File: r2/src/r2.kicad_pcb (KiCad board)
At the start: 4 copper layers, 110.2 x 145.8 mm, 234 parts, among them J1 532610271, J10 PJ-320D, J2 USB-C-12, J3 UJ2-AH-1-SMT, J4 TF-15x15, J5 AFC07-S24ECA-00, J6 DNP, J7 2x03-socket-2.54-through-board, J8 DNP, J9 532610271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

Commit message: Fabricate. End of history
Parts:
- moved FID1 22.8 mm to (-48.0, -129.4)
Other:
- board text added: "banellick"
- board text added: "jeffmakes"
- board text added: "malte"
- board text added: "norbert"
- board text added: "sourcing : nick completion : na origin : critical tooling : critical knowledge : critical understanding : unnecessary understanding : critical art : critical platform : mixed substrate : mixed credit : powers of two design ltd. custom : ernw insight gmbh. vendor : monad gottfried ltd., london assurance : critical opsec : redacted concept : critical synthesis : monad order : critical legal : gottf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"

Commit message: Remove stackup definition which was preventing file from  opening in my version of  kicad, for some unexplained reason
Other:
- board text added: "sourcing : nick origin : critical tooling : critical understanding : unnecessary understanding : critical art : critical platform : mixed substrate : mixed credit : powers of two design ltd. custom : ernw insight gmbh. vendor : monad gottfried ltd., london assurance : critical opsec : redacted concept : critical synthesis : monad legal : gottfried risk : powers of two design ltd. london support :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"
- board text removed: "sourcing : nick completion : na origin : critical tooling : critical knowledge : critical understanding : unnecessary understanding : critical art : critical platform : mixed substrate : mixed credit : powers of two design ltd. custom : ernw insight gmbh. vendor : monad gottfried ltd., london assurance : critical opsec : redacted concept : critical synthesis : monad order : critical legal : gottf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"

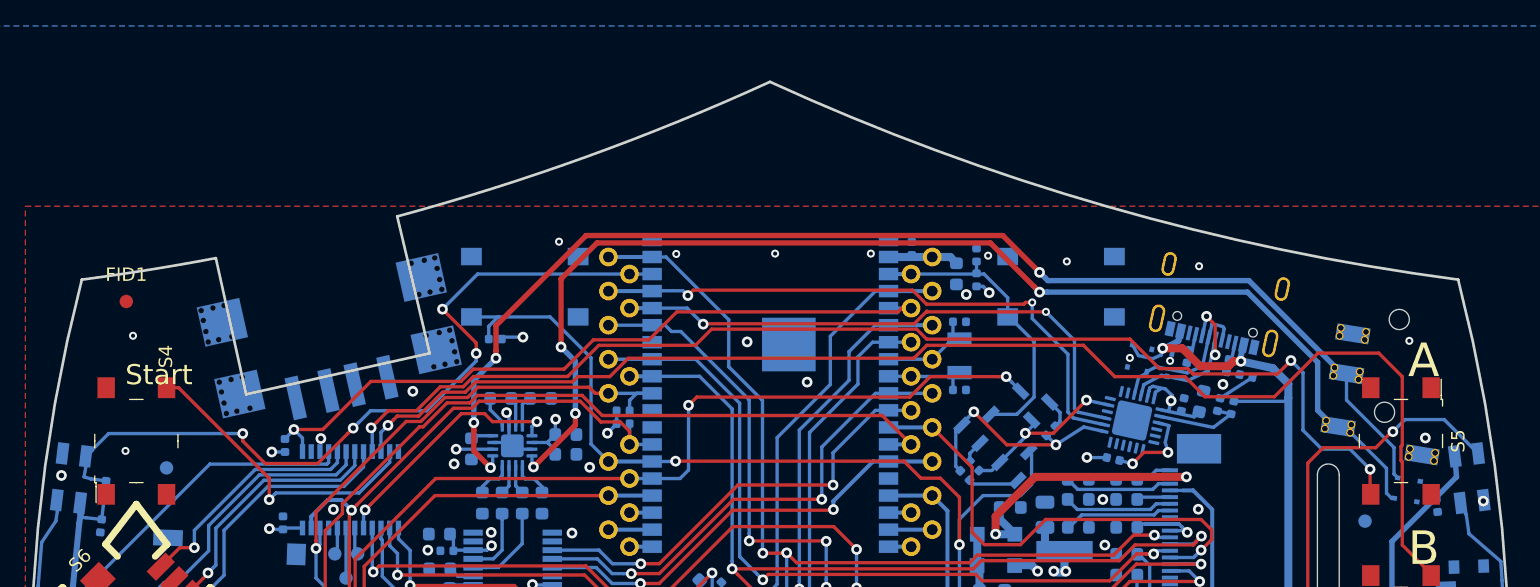
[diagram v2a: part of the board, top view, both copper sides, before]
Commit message: Updated USB-A footprint, board edge corrected to match
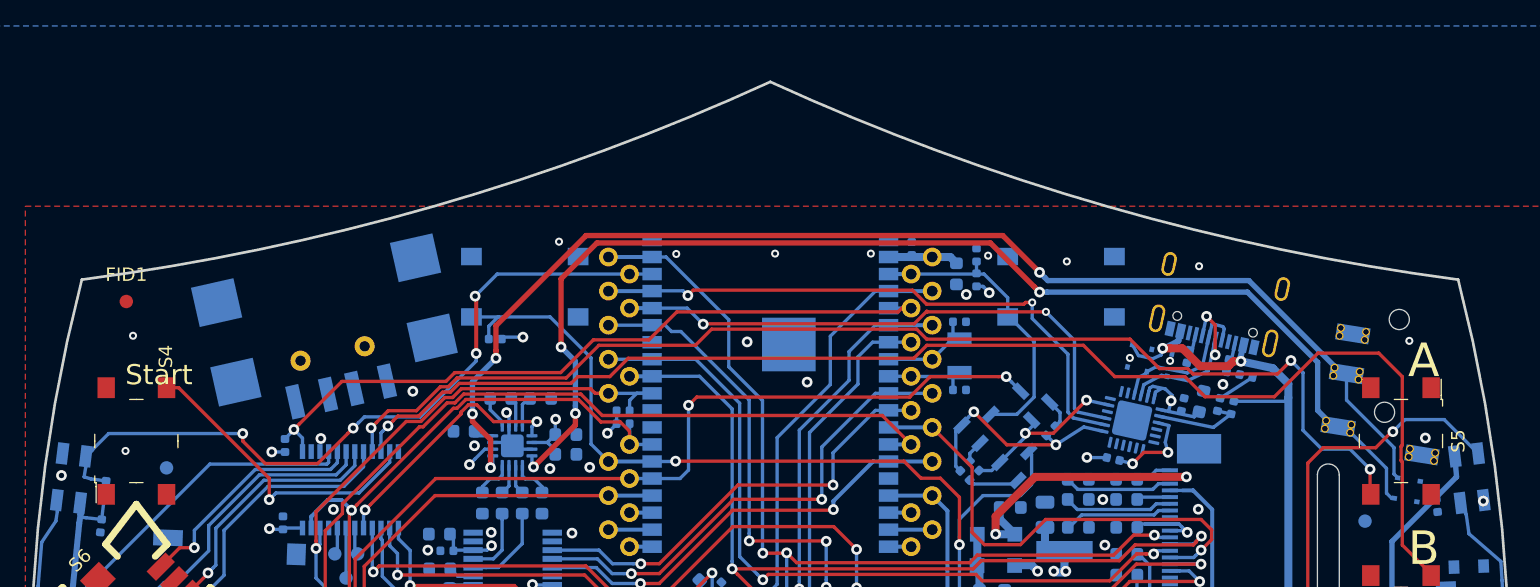
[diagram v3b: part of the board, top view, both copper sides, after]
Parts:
- J3: footprint jeffmakes-footprints:USB-A-short-body-in-cutout-type -> jeffmakes-footprints:USB-A-short-body
- moved J3 8.57 mm to (-32.6, -125.5)
- moved C87 1.42 mm to (-22.8, -119.7), turned to 0 degrees
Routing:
- net /LED_DIN: track 60.0 -> 57.4 mm
- net /AMP_EN: track 18.6 -> 19.2 mm
- net +3V3: track 1362.1 -> 1361.6 mm
- net GND: vias 168 -> 169
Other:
- outline, holes or cut-outs redrawn

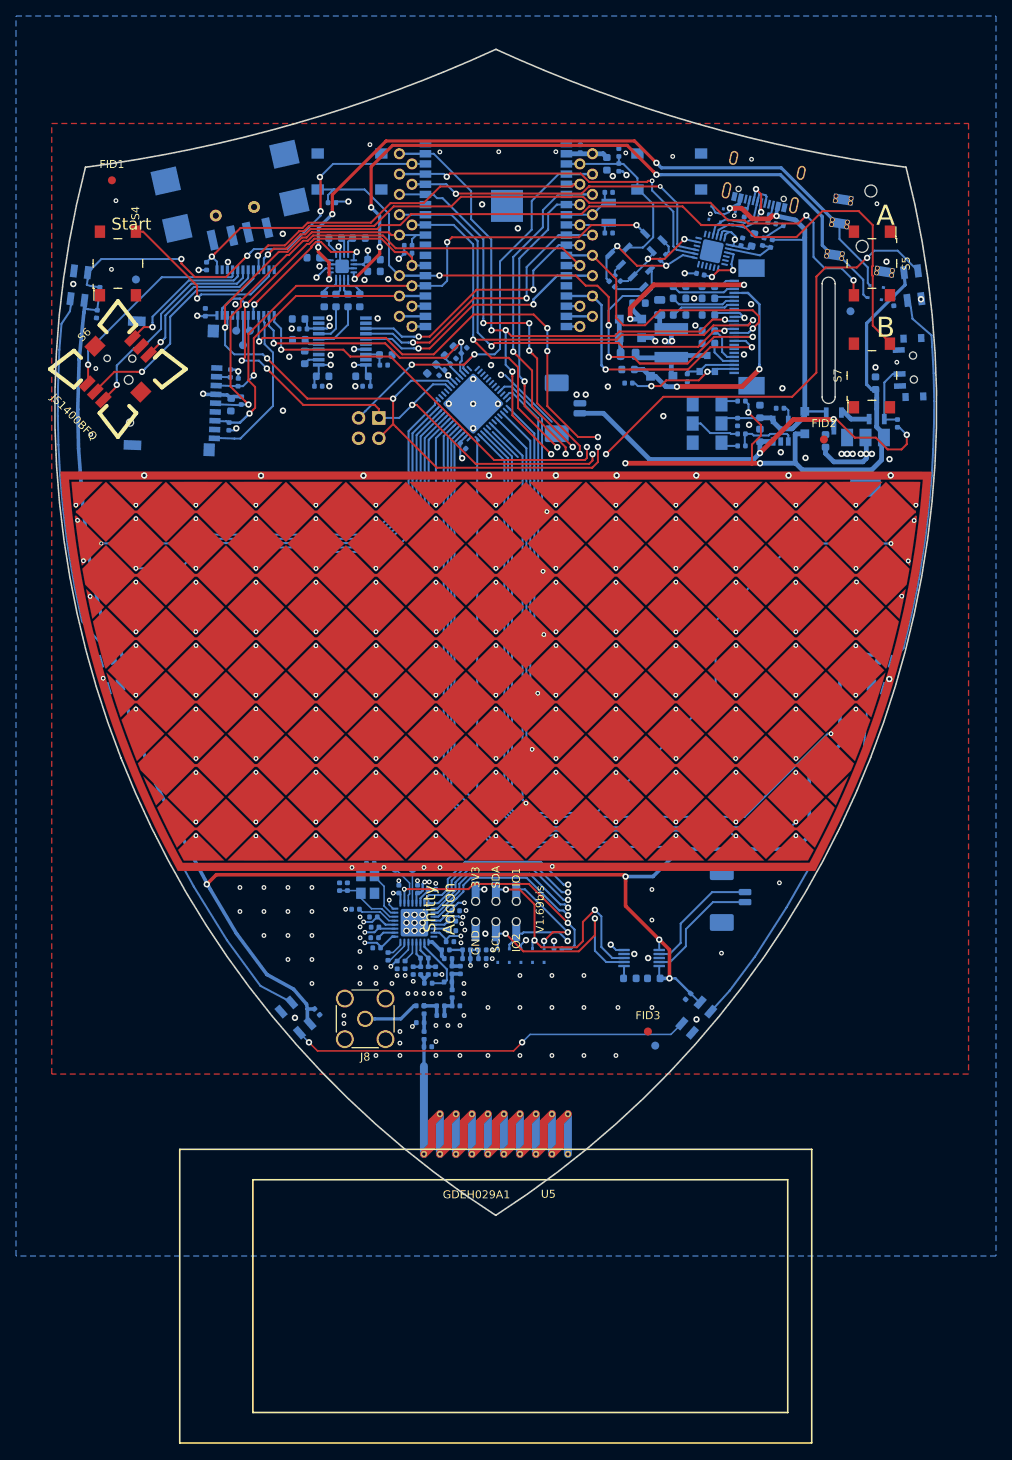
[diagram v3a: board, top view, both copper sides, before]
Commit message: DRC pass, silk for SAO
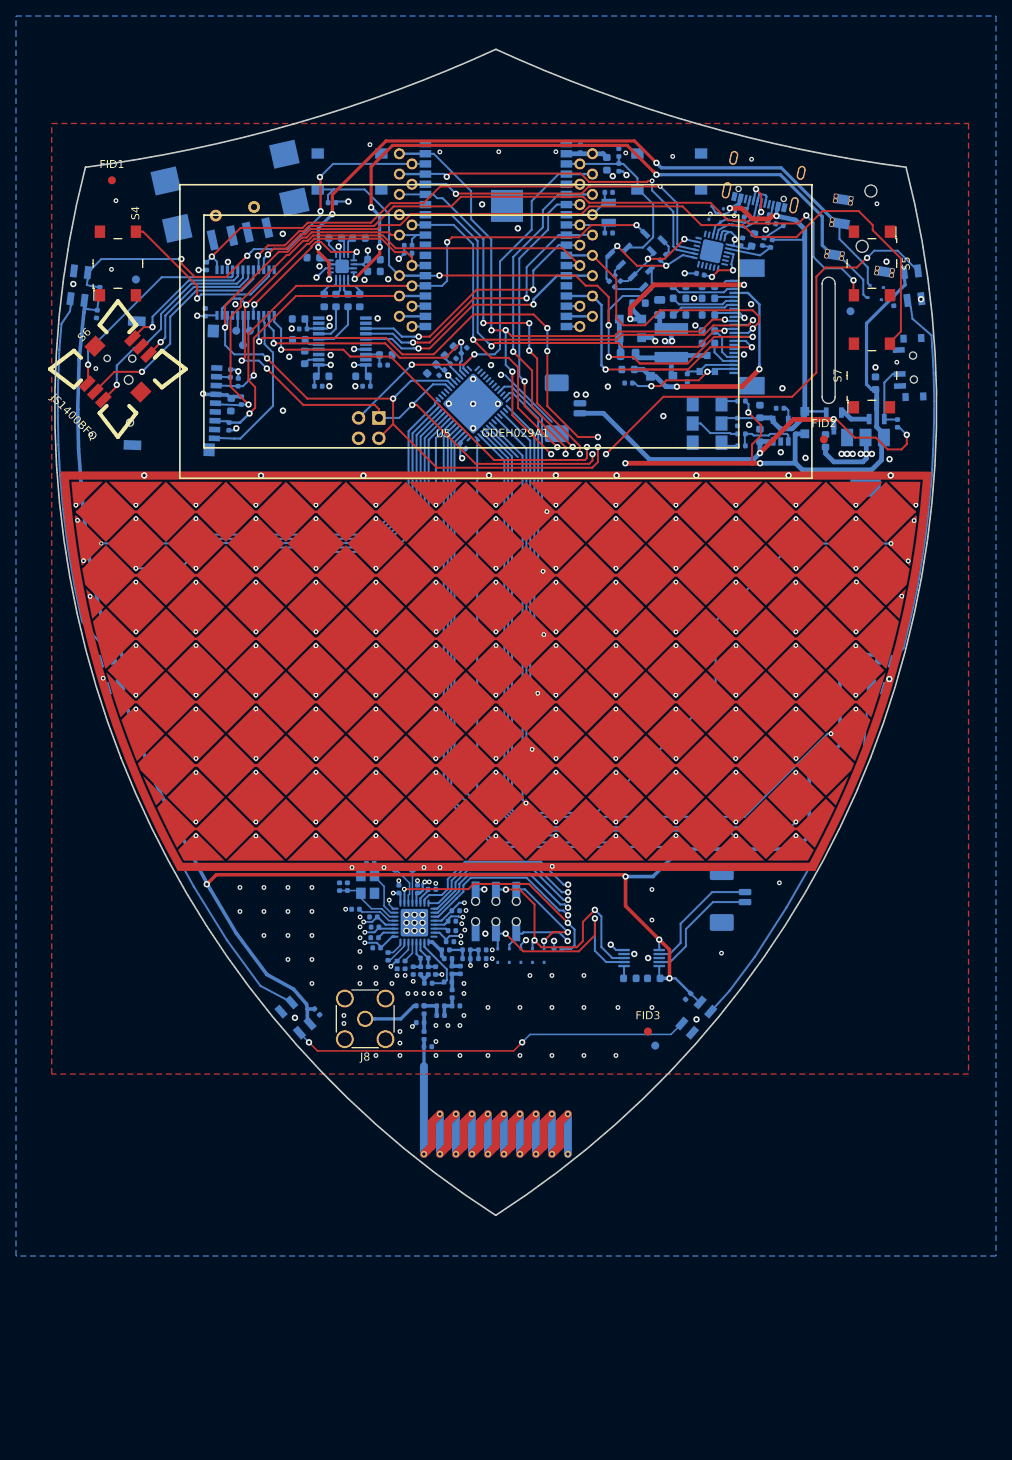
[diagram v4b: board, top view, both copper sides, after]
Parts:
- moved U5 120.6 mm to (0.00, -110.5), turned to 180 degrees
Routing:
- net /io_expander/BTN_B: track 99.7 -> 100.9 mm
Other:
- board text removed: "A"
- board text removed: "B"
- board text removed: "Start"

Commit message: Add credits
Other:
- board text added: "credits: badge.team norbert dr kl jim rgilton nick celina"
- board text removed: "banellick"
- board text removed: "jeffmakes"
- board text removed: "malte"
- board text removed: "norbert"
- board text removed: "sourcing : nick origin : critical tooling : critical understanding : unnecessary understanding : critical art : critical platform : mixed substrate : mixed credit : powers of two design ltd. custom : ernw insight gmbh. vendor : monad gottfried ltd., london assurance : critical opsec : redacted concept : critical synthesis : monad legal : gottfried risk : powers of two design ltd. london support :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"
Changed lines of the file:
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@@
   (general
     (thickness 1.6)
-    (drawings 87)
+    (drawings 60)
     (tracks 2399)
     (modules 234)
@@
     (32 "B.Adhes" user hide)
     (33 "F.Adhes" user hide)
-    (34 "B.Paste" user)
+    (34 "B.Paste" user hide)
     (35 "F.Paste" user hide)
     (36 "B.SilkS" user)
@@
     (45 "Margin" user hide)
     (46 "B.CrtYd" user hide)
-    (47 "F.CrtYd" user hide)
-    (48 "B.Fab" user hide)
-    (49 "F.Fab" user)
+    (47 "F.CrtYd" user)
+    (48 "B.Fab" user)
+    (49 "F.Fab" user hide)
   )
   (setup
@@
   )
   (gr_curve (pts (xy -51.312409 -131.029767) (xy -33.555051 -133.367724) (xy -16.268868 -138.335922) (xy 0 -145.7706)) (layer "Edge.Cuts") (width 0.2))
-  (gr_text "banellick" (at 0.8 -29) (layer "In1.Cu")
-    (effects (font (size 1 1) (thickness 0.1)) (justify mirror))
-  )
-  (gr_text "banellick" (at -25.8 -39.6) (layer "In1.Cu")
-    (effects (font (size 1 1) (thickness 0.1)) (justify mirror))
-  )
-  (gr_text "banellick" (at 19.8 -39) (layer "In1.Cu")
-    (effects (font (size 1 1) (thickness 0.1)) (justify mirror))
-  )
-  (gr_text "malte" (at 9.4 -31.6) (layer "In1.Cu")
-    (effects (font (size 1 1) (thickness 0.1)) (justify mirror))
-  )
-  (gr_text "malte" (at -20.2 -30.4) (layer "In1.Cu")
-    (effects (font (size 1 1) (thickness 0.1)) (justify mirror))
-  )
-  (gr_text "malte" (at -44.2 -125.4) (layer "In1.Cu")
-    (effects (font (size 1 1) (thickness 0.1)) (justify mirror))
-  )
-  (gr_text "malte" (at -38.8 -105.6) (layer "In1.Cu")
-    (effects (font (size 1 1) (thickness 0.1)) (justify mirror))
-  )
-  (gr_text "malte" (at 15.6 -102.4) (layer "In1.Cu")
-    (effects (font (size 1 1) (thickness 0.1)) (justify mirror))
-  )
-  (gr_text "malte" (at 35.8 -112.4) (layer "In1.Cu")
-    (effects (font (size 1 1) (thickness 0.1)) (justify mirror))
-  )
-  (gr_text "malte" (at -26.8 -96) (layer "In1.Cu")
-    (effects (font (size 1 1) (thickness 0.1)) (justify mirror))
-  )
-  (gr_text "sourcing : nick\norigin : critical\ntooling : critical\nunderstanding : unnecessary\nunderstanding : critical\nart : critical\nplatform : mixed\nsubstrate : mixed\ncredit : powers of two design ltd.\ncustom : ernw insight gmbh.\nvendor : monad gottfried ltd., london\nassurance : critical\nopsec : redacted\nconcept : critical\nsynthesis : monad\nlegal : gottfried\nrisk : powers of two design ltd. london\nsupport : Dr KL Jim\ndirection : diamond\ndesign : critical\nmistakes : admit\ndirection : critical\nproduction : ernw insight gmbh\ninfrastructure : critical\nlogistics : critical\nlogistics : kl\ntooling : critical\nlibrary : critical\ninspiration : mixed\ntitle : tr20-r2\nstack : badge.team\nfabrication : norbert\nfabrication : celina\nalarn : jeffmakes\nfabrication : mixed\nshelter : troublemaker\nhealthcare : kl\nnegligence : redacted\nlegal : monad gottfried ltd.\ncredit : alan\nsupport : alan\nsupport : mixed\narchitecture : badge.team\ndrivers : jeffmakes\ndrivers : hnzlmnn\nsystem : hnzlmnn\ndrivers : espressif" (at -51.2 -123.4) (layer "In1.Cu")
-    (effects (font (size 0.1 0.1) (thickness 0.01)) (justify left))
-  )
-  (gr_text "jeffmakes" (at 2.6 -46) (layer "In1.Cu")
-    (effects (font (size 1 1) (thickness 0.1)) (justify mirror))
-  )
-  (gr_text "jeffmakes" (at 45.8 -55) (layer "In1.Cu")
-    (effects (font (size 1 1) (thickness 0.1)) (justify mirror))
-  )
-  (gr_text "norbert" (at -0.8 -22.6) (layer "In1.Cu")
-    (effects (font (size 1 1) (thickness 0.1)) (justify mirror))
-  )
-  (gr_text "norbert" (at 24.8 -34.6) (layer "In1.Cu")
-    (effects (font (size 1 1) (thickness 0.1)) (justify mirror))
-  )
-  (gr_text "norbert" (at -24 -36.2) (layer "In1.Cu")
-    (effects (font (size 1 1) (thickness 0.1)) (justify mirror))
-  )
-  (gr_text "norbert" (at 27.2 -40.2) (layer "In1.Cu")
-    (effects (font (size 1 1) (thickness 0.1)) (justify mirror))
-  )
-  (gr_text "norbert" (at 23.1 -59.7) (layer "In1.Cu")
-    (effects (font (size 1 1) (thickness 0.1)) (justify mirror))
-  )
-  (gr_text "norbert" (at 23.3 -96.4) (layer "In1.Cu")
-    (effects (font (size 1 1) (thickness 0.1)) (justify mirror))
-  )
-  (gr_text "norbert" (at 47.9 -100.5) (layer "In1.Cu")
-    (effects (font (size 1 1) (thickness 0.1)) (justify mirror))
-  )
-  (gr_text "norbert" (at 3.7 -98.1) (layer "In1.Cu")
-    (effects (font (size 1 1) (thickness 0.1)) (justify mirror))
-  )
-  (gr_text "norbert" (at 35.8 -118.4) (layer "In1.Cu")
-    (effects (font (size 1 1) (thickness 0.1)) (justify mirror))
-  )
-  (gr_text "norbert" (at 5.8 -126.5) (layer "In1.Cu")
-    (effects (font (size 1 1) (thickness 0.1)) (justify mirror))
-  )
-  (gr_text "jeffmakes" (at 21.6 -85.1) (layer "In1.Cu")
-    (effects (font (size 1 1) (thickness 0.1)) (justify mirror))
-  )
-  (gr_text "jeffmakes" (at 2.5 -120) (layer "In1.Cu")
-    (effects (font (size 1 1) (thickness 0.1)) (justify mirror))
-  )
-  (gr_text "jeffmakes" (at 3.3 -131.1) (layer "In1.Cu")
-    (effects (font (size 1 1) (thickness 0.1)) (justify mirror))
-  )
-  (gr_text "jeffmakes" (at -40.1 -97.7) (layer "In1.Cu")
-    (effects (font (size 1 1) (thickness 0.1)) (justify mirror))
-  )
-  (gr_text "jeffmakes" (at 0.6 -59.4) (layer "In1.Cu")
-    (effects (font (size 1 1) (thickness 0.1)) (justify mirror))
+  (gr_text "credits:\n badge.team\n norbert\n dr kl jim\n rgilton\n nick\n celina\n\n\n\n" (at -19.35 -34.4) (layer "B.SilkS")
+    (effects (font (size 1.2 1.2) (thickness 0.2)) (justify left mirror))
   )
   (gr_curve (pts (xy -46.883119 -57.219047) (xy -37.674227 -33.69504) (xy -21.276246 -13.677277) (xy -0.0254 -0.017693)) (layer "Edge.Cuts") (width 0.2))
@@
   (gr_curve (pts (xy 51.263362 -131.029767) (xy 33.555051 -133.367724) (xy 16.268868 -138.335922) (xy 0 -145.7706)) (layer "Edge.Cuts") (width 0.2))
   (gr_text "x-ray\nchallenge" (at 9.75 -26) (layer "B.SilkS")
-    (effects (font (size 1 1) (thickness 0.15)) (justify mirror))
+    (effects (font (size 1 1) (thickness 0.2)) (justify mirror))
   )
   (gr_line (start 2.75 -23.25) (end 2.75 -25) (layer "B.SilkS") (width 0.3))
@@
   (gr_line (start -50.292 -121.9962) (end -50.292 -115.951) (layer "F.Fab") (width 0.1))
   (gr_text "V1.69bis" (at 10.55 -37.9 90) (layer "B.SilkS")
-    (effects (font (size 1 1) (thickness 0.15)))
+    (effects (font (size 1 1) (thickness 0.2)))
   )
   (gr_text "3V3" (at -2.45 -43.3 90) (layer "B.SilkS")
-    (effects (font (size 1 1) (thickness 0.15)))
+    (effects (font (size 1 1) (thickness 0.2)))
   )
   (gr_text "IO1" (at 2.6 -43.15 90) (layer "B.SilkS")
-    (effects (font (size 1 1) (thickness 0.15)))
+    (effects (font (size 1 1) (thickness 0.2)))
   )
   (gr_text "SDA" (at 0 -43.3 90) (layer "B.SilkS")
-    (effects (font (size 1 1) (thickness 0.15)))
+    (effects (font (size 1 1) (thickness 0.2)))
   )
   (gr_text "IO2" (at 2.4 -29.45 90) (layer "B.SilkS")
-    (effects (font (size 1 1) (thickness 0.15)))
+    (effects (font (size 1 1) (thickness 0.2)))
   )
   (gr_text "SCL" (at -0.1 -29.55 90) (layer "B.SilkS")
-    (effects (font (size 1 1) (thickness 0.15)))
+    (effects (font (size 1 1) (thickness 0.2)))
   )
   (gr_text "GND" (at -2.6 -29.5 90) (layer "B.SilkS")
-    (effects (font (size 1 1) (thickness 0.15)))
+    (effects (font (size 1 1) (thickness 0.2)))
   )
   (gr_text "AUDIO" (at 50.6476 -123.0376 81) (layer "Cmts.User")
